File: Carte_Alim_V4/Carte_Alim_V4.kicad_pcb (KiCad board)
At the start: 2 copper layers, 61 parts, among them J1 BAT_IN, J10 12VC, J11 12VC, J12 12VC, J13 12VP, J14 12VP, J15 12VP, J16 12VP, J17 12VP, J18 12VP, J19 5VC, J2 BAT_IN, J20 5V_CAN, J21 5VC, J22 5V_CAN, J23 5VC, J24 5V_CAN, J25 5VC, J26 5V_CAN, J27 5VP, J28 5VP, J29 5VP, J3 MOT_OUT, J30 5VP, J31 5VP, J32 5VP, J4 MOT_OUT, J5 MOT_OUT, J6 MOT_OUT, J7 12VC, J8 12VC, J9 12VC, U1 LM2678S-5.0, U2 LM2678S-12

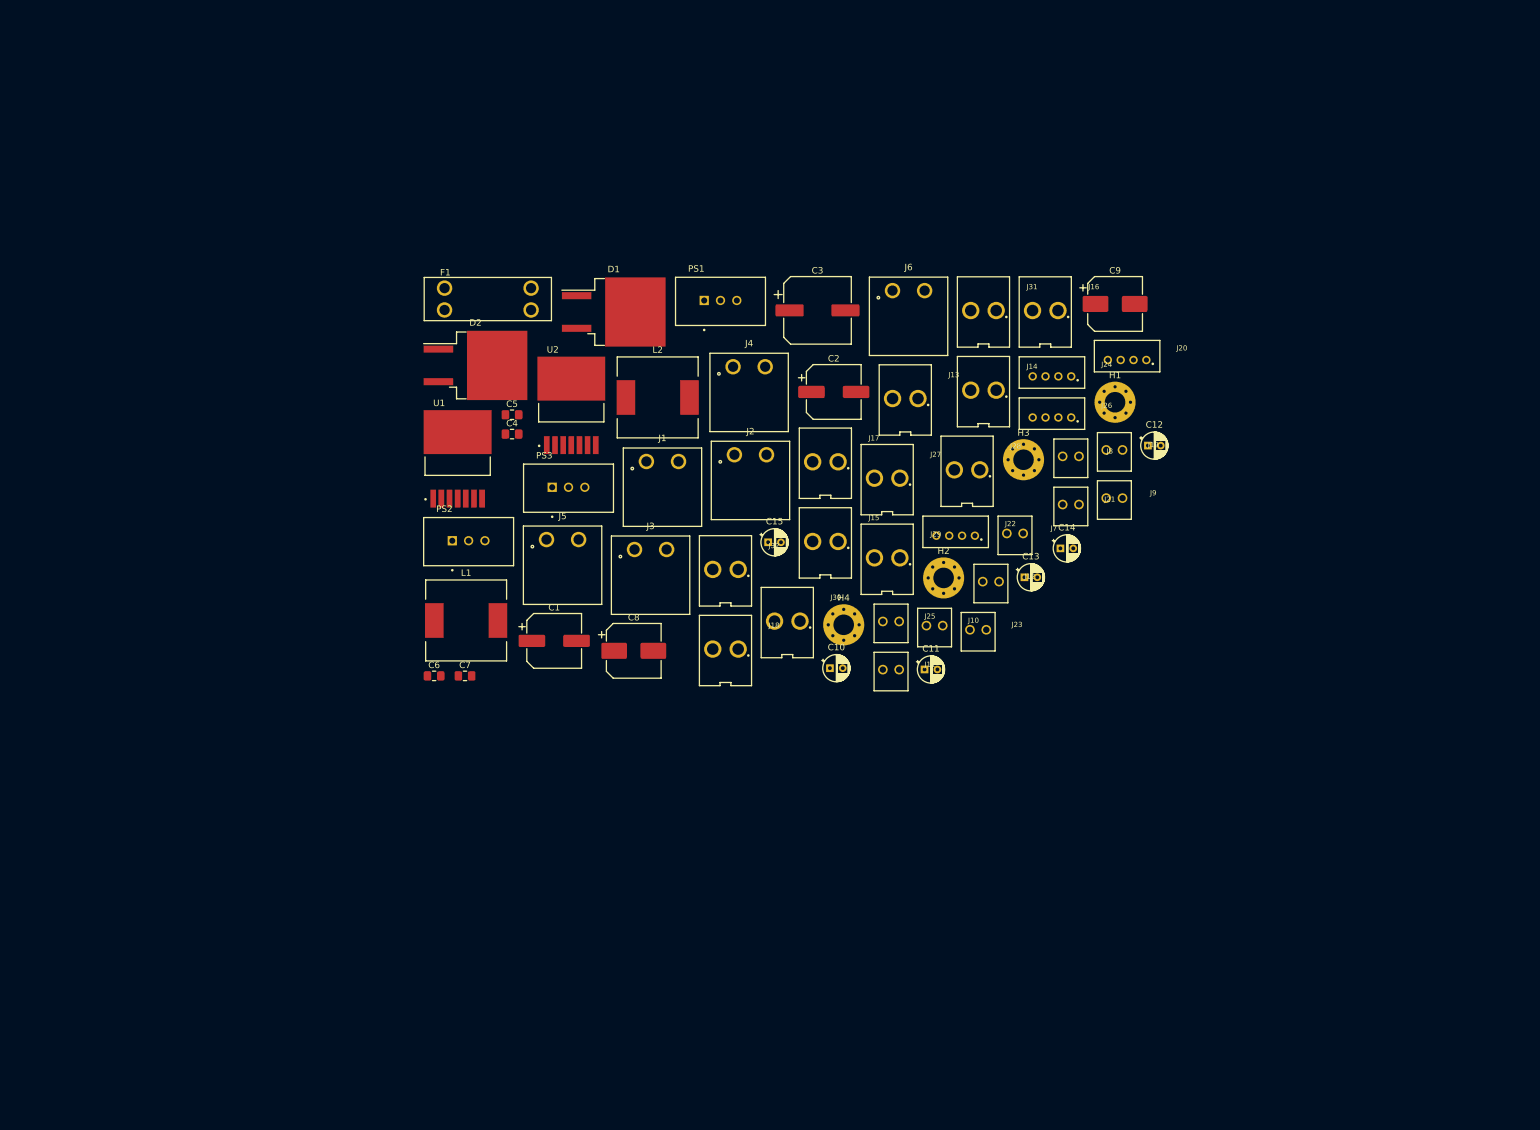
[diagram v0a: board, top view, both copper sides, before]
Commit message: IO prete, Pompe finir sérigraphie, Alim+AX12 à faire
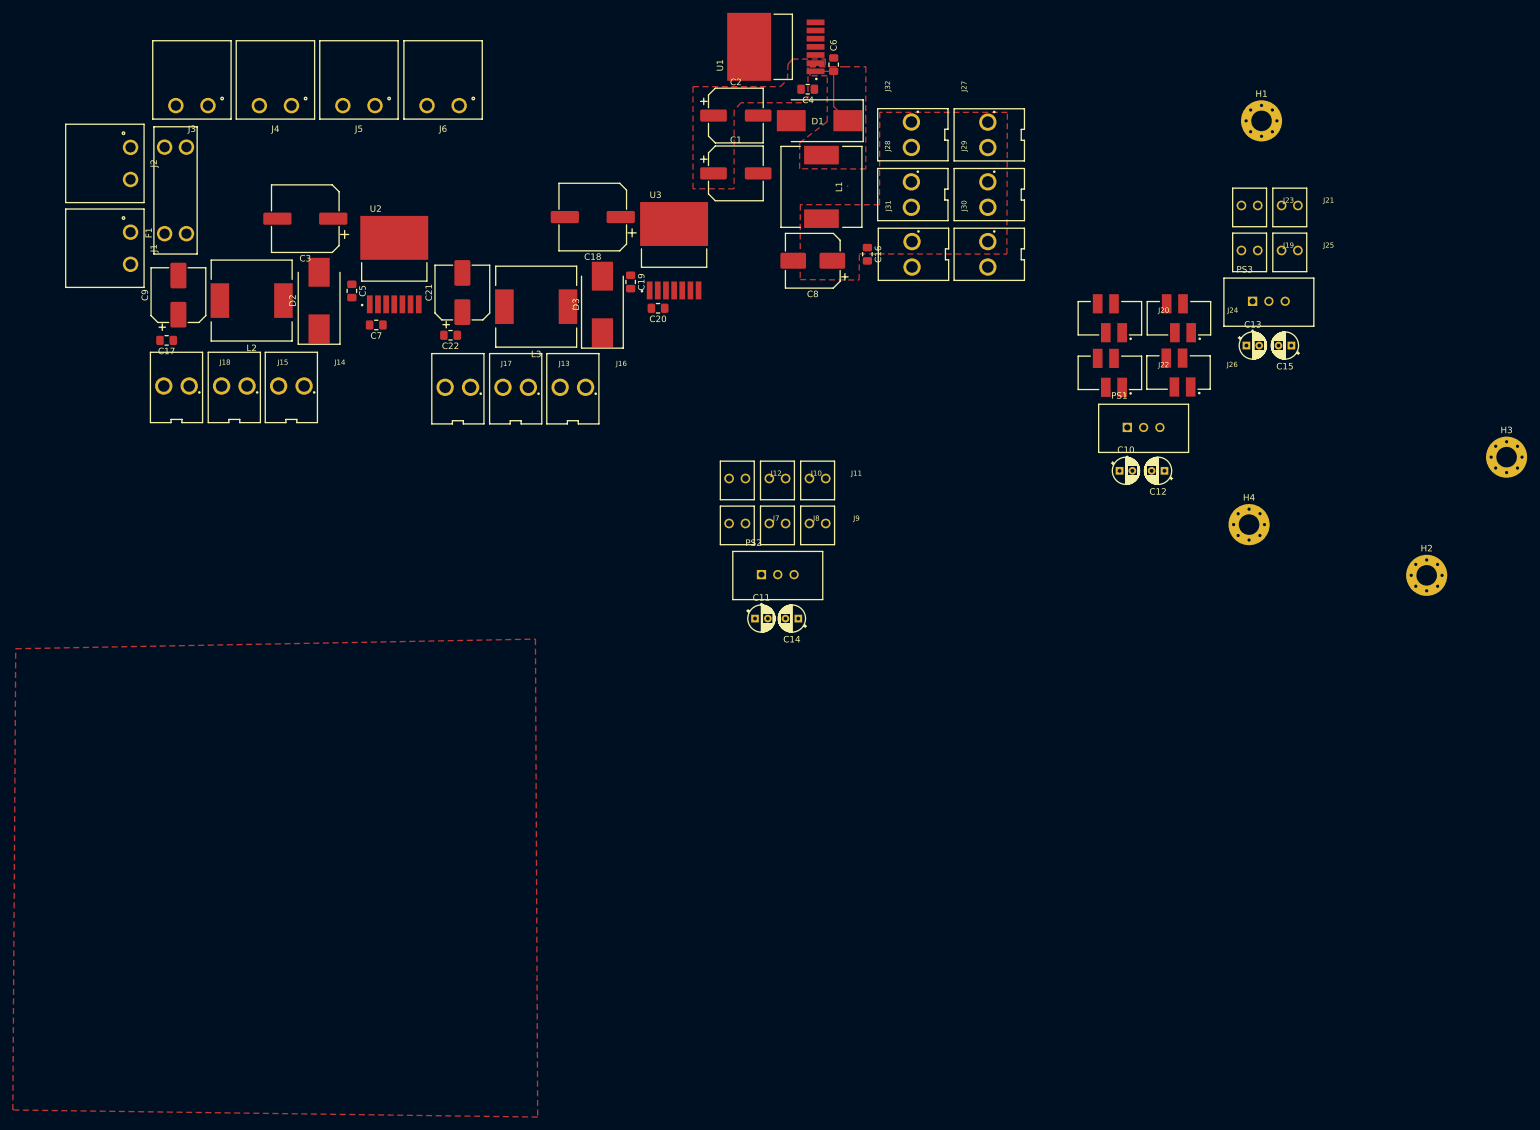
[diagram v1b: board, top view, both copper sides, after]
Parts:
- added C16: 100n, Capacitor_SMD:C_0805_2012Metric_Pad1.18x1.45mm_HandSolder, F.Cu at (165.0, 48.3)
- added C17: 100n, Capacitor_SMD:C_0805_2012Metric_Pad1.18x1.45mm_HandSolder, F.Cu at (55.9, 61.7)
- added C18: 330u, Capacitor_SMD:CP_Elec_10x12.6, F.Cu at (122.2, 42.5)
- added C19: 100n, Capacitor_SMD:C_0805_2012Metric_Pad1.18x1.45mm_HandSolder, F.Cu at (128.2, 52.6)
- added C20: 10n, Capacitor_SMD:C_0805_2012Metric_Pad1.18x1.45mm_HandSolder, F.Cu at (132.4, 56.7)
- added C21: 330u, Capacitor_SMD:CP_Elec_8x6.2, F.Cu at (102.0, 54.2)
- added C22: 100n, Capacitor_SMD:C_0805_2012Metric_Pad1.18x1.45mm_HandSolder, F.Cu at (100.1, 60.9)
- added D3: S8KC-13, Diode_SMD:D_SMC_Handsoldering, F.Cu at (123.8, 56.1)
- added L3: MSS1210-153MED, Inductor_SMD:L_12x12mm_H8mm, F.Cu at (113.4, 56.5)
- added U3: LM2678S-12, AREA_lib_composant:TO127P1435X464-8N, F.Cu at (134.9, 47.7)
- D1, D2: value VB20100S-E3/8W -> S8KC-13; footprint Package_TO_SOT_SMD:TO-263-2_TabPin1 -> Diode_SMD:D_SMC_Handsoldering
- J20, J22, J24, J26: footprint AREA_lib_Connector:Wuerth_2mm_4pin_62000411622 -> AREA_lib_Connector:690367290476
- moved C9 145.8 mm to (57.8, 54.6), turned to 90 degrees
- moved C6 113.7 mm to (159.8, 18.8), turned to 270 degrees
- moved PS3 112.8 mm to (227.5, 55.8)
- moved J14 107.7 mm to (75.3, 69.3)
- moved J2 106.6 mm to (50.3, 34.1), turned to 270 degrees
- moved J3 99.4 mm to (59.9, 25.1), turned to 180 degrees
- moved J15 95.1 mm to (66.5, 69.3)
- moved J18 94.8 mm to (57.5, 69.3)
- moved J1 89.2 mm to (50.3, 47.4), turned to 270 degrees
- moved L1 87.3 mm to (157.8, 37.8), turned to 270 degrees
- moved C15 87.0 mm to (231.0, 62.5), turned to 180 degrees
- moved J25 84.8 mm to (230.8, 48.0)
- moved J4 84.2 mm to (72.8, 25.1), turned to 180 degrees
- moved U1 81.0 mm to (150.8, 16.0), turned to 90 degrees
- moved C3 81.0 mm to (77.5, 42.8), turned to 180 degrees
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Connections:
- C3 pad 2: Net-(C3-Pad2) -> GND
- C5 pad 2: Net-(C3-Pad2) -> GND
- C9 pad 2: Net-(C3-Pad2) -> GND
- D2 pad 2: Net-(C3-Pad2) -> GND
- J3 pad 1: +BATT -> +24V
- J4 pad 1: +BATT -> +24V
- J5 pad 1: +BATT -> +24V
- J6 pad 1: +BATT -> +24V
- U2 pad 4: Net-(C3-Pad2) -> GND
- U2 pad 8: Net-(C3-Pad2) -> GND
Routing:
- net Net-(C6-Pad2): track 0.00 -> 11.5 mm
- added copper zone on F.Cu, net +24V
- added copper zone on F.Cu, net +5P
- added copper zone on F.Cu, net GND
- added copper zone on F.Cu, net Net-(C6-Pad2)
